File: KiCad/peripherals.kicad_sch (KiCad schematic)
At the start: 36 parts, among them IC1 MIC5350-SGYMT-TR, J1 Conn_02x06_Counter_Clockwise, J2 USB_C_Receptacle_USB2.0_14P, J3 Conn_01x07, J4 Conn_01x06, J6 Conn_02x11_Counter_Clockwise, U1 EM008LX, U2 EM008LX, U3 EM008LX, X1 2x5 0.05" SWD

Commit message: update draft to 11/13 version
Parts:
- removed J6: Conn_02x11_Counter_Clockwise, Connector_Hirose:Hirose_DF11-22DP-2DSA_2x11_P2.00mm_Vertical, symbol Connector_Generic:Conn_02x11_Counter_Clockwise
- added C5, C6, C7, C8: 0.1 uF, Capacitor_SMD:C_0201_0603Metric, symbol Device:C
- added R16, R17: 10K, Resistor_SMD:R_0603_1608Metric, symbol Device:R
- added U5, U6: TXS0108EPW, Package_SO:TSSOP-20_4.4x6.5mm_P0.65mm, symbol Logic_LevelTranslator:TXS0108EPW
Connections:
- net 1V8: now also R4.2, R5.2, R6.2, C5.1, C8.1, U5.2 (VCCA), U6.2 (VCCA); no longer R4.1, R5.1, R6.1
- net 3V3: now also C6.1, C7.1, U5.19 (VCCB), U6.19 (VCCB)
- net GND: now also C5.2, C6.2, C7.2, C8.2, R16.2, R17.2, U5.11 (GND), U6.11 (GND)
- net PC04: now also U5.20 (B1); no longer U1.1 (~{CS})
- net PC05: now also U5.18 (B2); no longer R4.2, U1.7 (IO3/~{RESET})
- net PC06: now also U5.17 (B3); no longer U2.1 (~{CS})
- net PC07: now also U5.16 (B4); no longer R5.2, U2.7 (IO3/~{RESET})
- net PC10: now also U5.15 (B5); no longer R6.2, U3.7 (IO3/~{RESET})
- net PC11: now also U5.14 (B6); no longer U3.1 (~{CS})
- net PC12: now also U6.14 (B6); no longer R3.2, U3.3 (~{WP}/IO2)
- net PC14: now also U6.15 (B5); no longer R1.2, U1.3 (~{WP}/IO2)
- net PC15: now also U6.16 (B4); no longer R2.2, U2.3 (~{WP}/IO2)
- net PD08 (MOSI): now also U6.17 (B3); no longer U1.5 (IO0), U2.5 (IO0), U3.5 (IO0)
- net PD09 (SCK): now also U6.18 (B2); no longer U1.6 (CK), U2.6 (CK), U3.6 (CK)
- net PD11 (MISO): now also U6.20 (B1); no longer U1.2 (IO1), U2.2 (IO1), U3.2 (IO1)
- new net: R16.1, U5.10 (OE)
- new net: R17.1, U6.10 (OE)
- new net PC04 1V8: U1.1 (~{CS}), U5.1 (A1)
- new net PC05 1V8: R4.1, U1.7 (IO3/~{RESET}), U5.3 (A2)
- new net PC06 1V8: U2.1 (~{CS}), U5.4 (A3)
- new net PC07 1V8: R5.1, U2.7 (IO3/~{RESET}), U5.5 (A4)
- new net PC10 1V8: R6.1, U3.7 (IO3/~{RESET}), U5.6 (A5)
- new net PC11 1V8: U3.1 (~{CS}), U5.7 (A6)
- new net PC12 1V8: R3.2, U3.3 (~{WP}/IO2), U6.7 (A6)
- new net PC14 1V8: R1.2, U1.3 (~{WP}/IO2), U6.6 (A5)
- new net PC15 1V8: R2.2, U2.3 (~{WP}/IO2), U6.5 (A4)
- new net PD08 (MOSI) 1V8: U1.5 (IO0), U2.5 (IO0), U3.5 (IO0), U6.4 (A3)
- new net PD09 (SCK) 1V8: U1.6 (CK), U2.6 (CK), U3.6 (CK), U6.3 (A2)
- new net PD11 (MISO) 1V8: U1.2 (IO1), U2.2 (IO1), U3.2 (IO1), U6.1 (A1)
- no-connect marks 3 -> 11
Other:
- note removed: "PHOTODIODES"
- moved on the sheet: C1, H1, H2, H3, H4, J1, J2, ON1, R8, U1, U2, U3

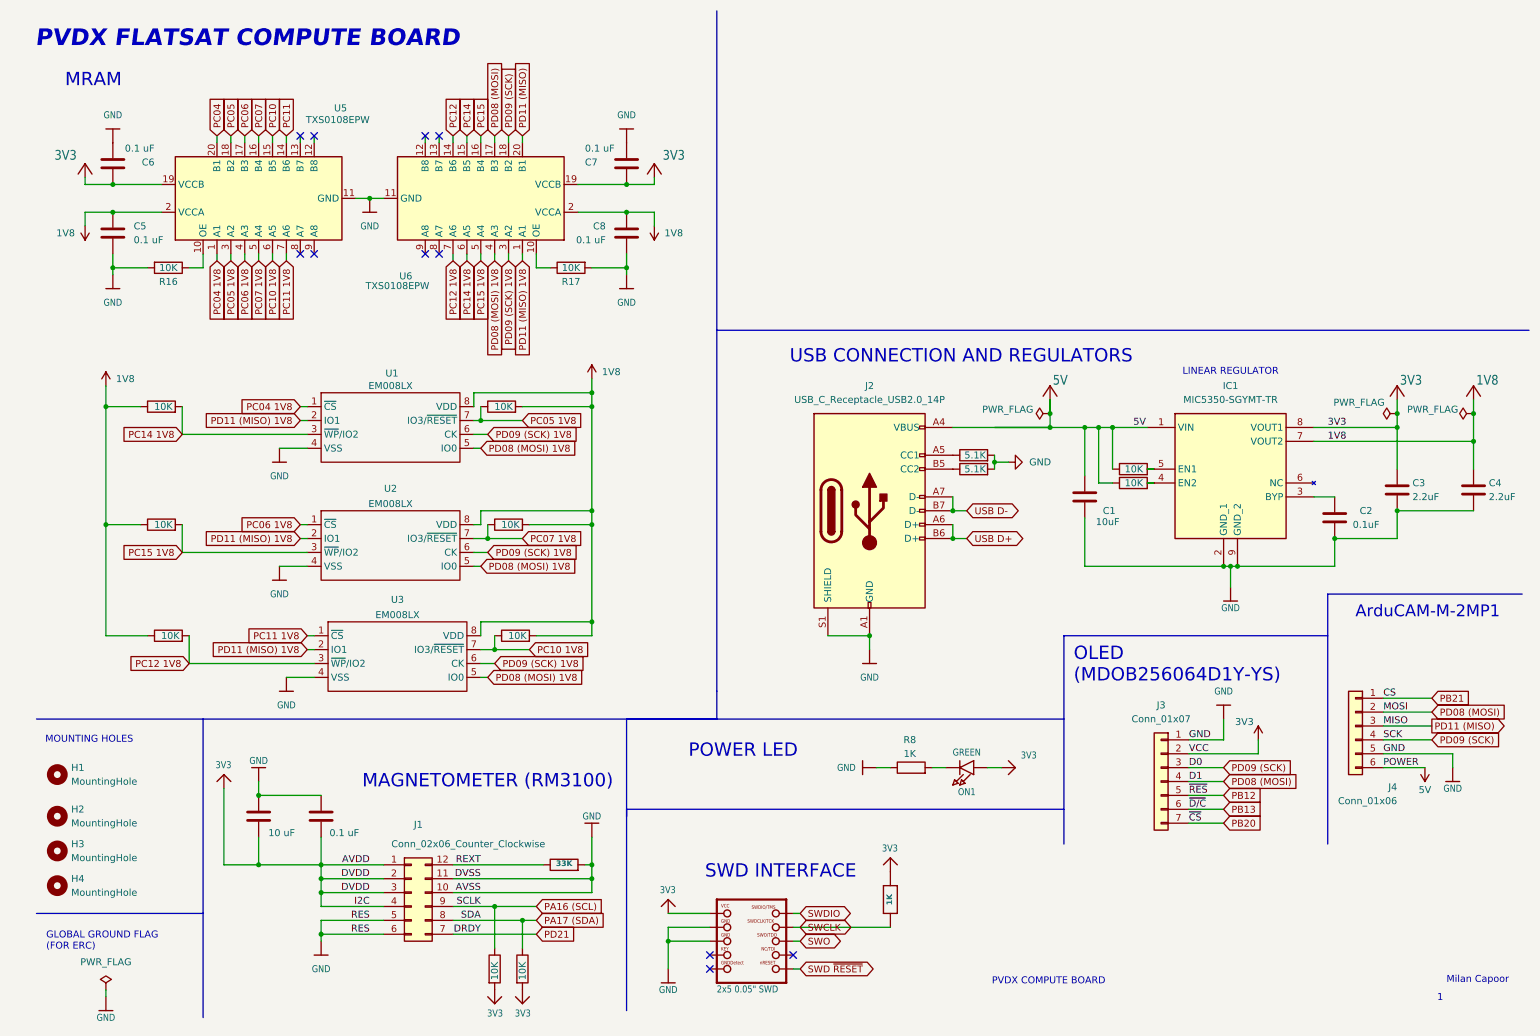
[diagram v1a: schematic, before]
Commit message: updated pins to match new spec and exposed all pins
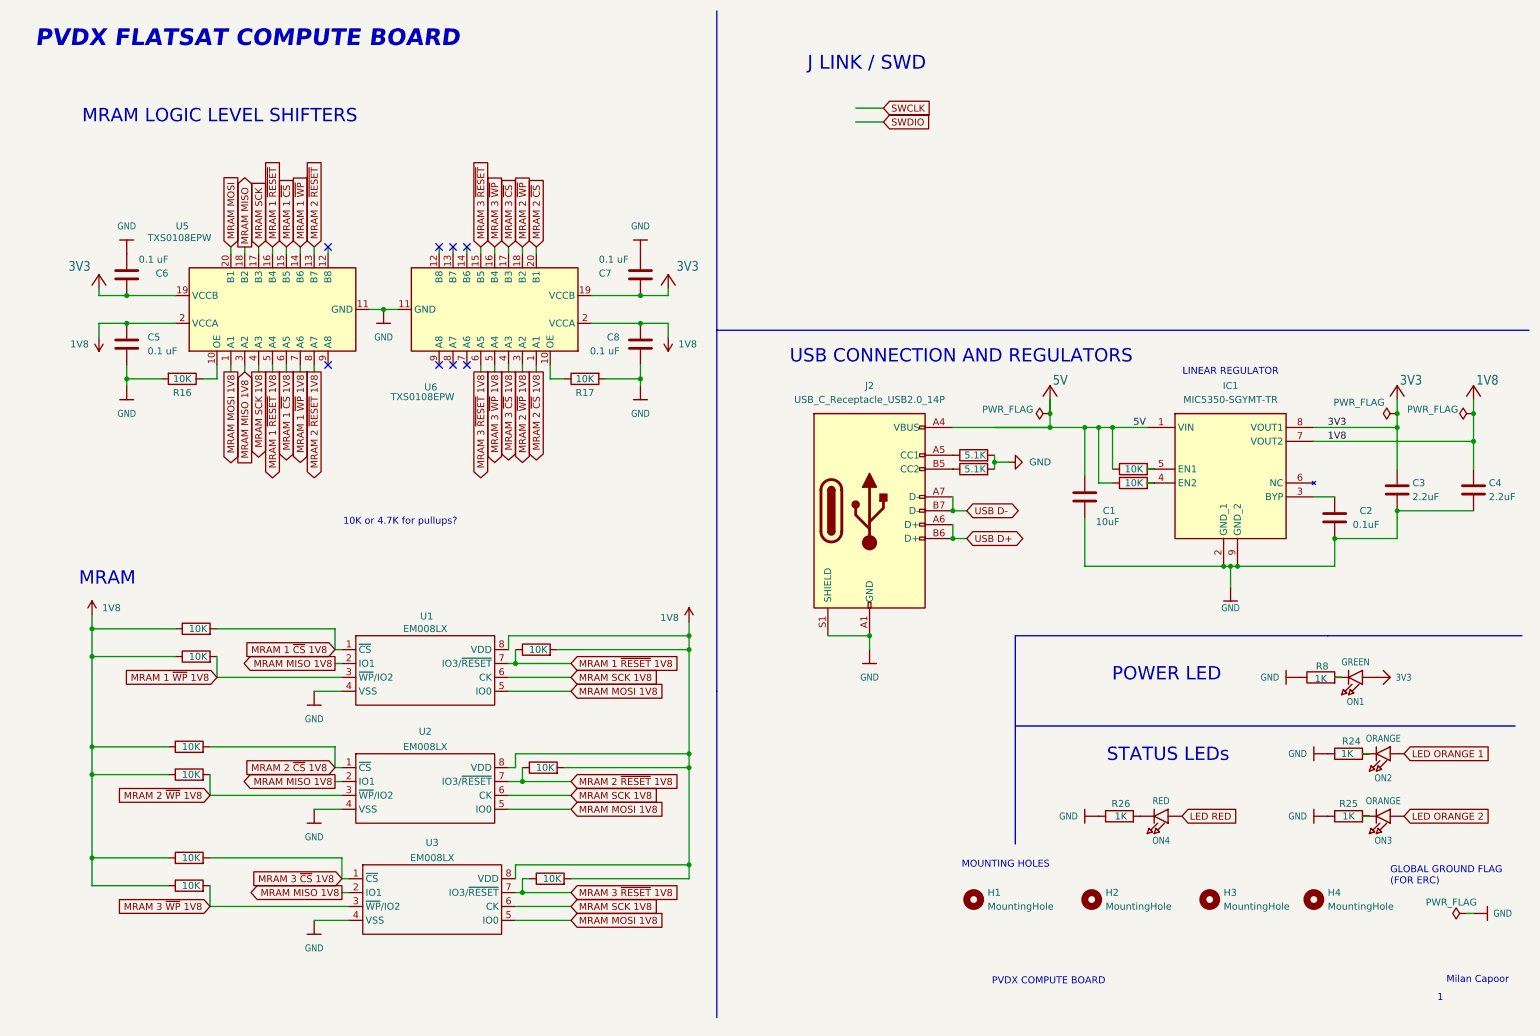
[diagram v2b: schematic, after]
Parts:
- removed CIN1: 10 uF, Capacitor_SMD:C_0201_0603Metric, symbol Device:C
- removed CIN2: 0.1 uF, Capacitor_SMD:C_0201_0603Metric, symbol Device:C
- removed J1: Conn_02x06_Counter_Clockwise, Connector_Harwin:Harwin_Gecko-G125-FVX1205L0X_2x06_P1.25mm_Vertical, symbol Connector_Generic:Conn_02x06_Counter_Clockwise
- removed J3: Conn_01x07, Connector_Molex:Molex_Micro-Latch_53253-0770_1x07_P2.00mm_Vertical, symbol Connector_Generic:Conn_01x07
- removed J4: Conn_01x06, Connector_Molex:Molex_Micro-Latch_53253-0670_1x06_P2.00mm_Vertical, symbol Connector_Generic:Conn_01x06
- removed R11: 1K, Resistor_SMD:R_0603_1608Metric, symbol Adafruit Grand Central M4 Express rev B-eagle-import:RESISTOR_0603_NOOUT
- removed R14, R15: 10K, Resistor_SMD:R_0603_1608Metric, symbol Device:R
- removed R7: 33K, Resistor_SMD:R_0603_1608Metric, symbol Device:R
- removed X1: 2x5 0.05" SWD, Adafruit Grand Central M4 Express rev B:2X05_1.27MM_BOX_POSTS, symbol Adafruit Grand Central M4 Express rev B-eagle-import:JTAG-CORTEXBOXPOSTS
- added ON2, ON3: ORANGE, Adafruit Grand Central M4 Express rev B:CHIPLED_0805_NOOUTLINE, symbol Adafruit Grand Central M4 Express rev B-eagle-import:LED0805_NOOUTLINE
- added ON4: RED, Adafruit Grand Central M4 Express rev B:CHIPLED_0805_NOOUTLINE, symbol Adafruit Grand Central M4 Express rev B-eagle-import:LED0805_NOOUTLINE
- added R11, R22, R23: 10K, Resistor_SMD:R_0603_1608Metric, symbol Device:R
- added R24, R25, R26: 1K, Resistor_SMD:R_0603_1608Metric, symbol Device:R
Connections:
- net 1V8: now also R11.1, R22.1, R23.1
- net GND: now also R24.1, R25.1, R26.1
- net MRAM 2 ~{RESET}: now reaches U5.13 (B7)
- net MRAM 2 ~{RESET} 1V8: now reaches U5.8 (A7)
- net MRAM 2 ~{RESET} 1V8: now also R5.1, U2.7 (IO3/~{RESET})
- net PC04 renamed MRAM MOSI
- net PC04 1V8 renamed MRAM 1 ~{CS} 1V8
- net MRAM 1 ~{CS} 1V8: now also U5.6 (A5), R11.2; no longer U5.1 (A1)
- net PC05 renamed MRAM MISO
- net PC05 1V8 renamed MRAM 1 ~{RESET} 1V8
- net MRAM 1 ~{RESET} 1V8: now also U5.5 (A4); no longer U5.3 (A2)
- net PC06 renamed MRAM SCK
- net PC06 1V8 renamed MRAM 2 ~{CS} 1V8
- net MRAM 2 ~{CS} 1V8: now also U6.1 (A1), R22.2; no longer U5.4 (A3)
- net PC07 renamed MRAM 1 ~{RESET}
- removed net PC07 1V8: R5.1, U2.7 (IO3/~{RESET}), U5.5 (A4)
- net PC10 renamed MRAM 1 ~{CS}
- net PC10 1V8 renamed MRAM 3 ~{RESET} 1V8
- net MRAM 3 ~{RESET} 1V8: now also U6.6 (A5); no longer U5.6 (A5)
- net PC11 renamed MRAM 1 ~{WP}
- net PC11 1V8 renamed MRAM 1 ~{WP} 1V8
- net MRAM 1 ~{WP} 1V8: now also R1.2, U1.3 (~{WP}/IO2); no longer U3.1 (~{CS})
- net PC12: no longer names the net of U6.14 (B6)
- net PC12 1V8 renamed MRAM 3 ~{WP} 1V8
- net MRAM 3 ~{WP} 1V8: now also U6.5 (A4); no longer U6.7 (A6)
- net PC14 renamed MRAM 3 ~{RESET}
- removed net PC14 1V8: R1.2, U1.3 (~{WP}/IO2), U6.6 (A5)
- net PC15 renamed MRAM 3 ~{WP}
- net PC15 1V8 renamed MRAM 2 ~{WP} 1V8
- net MRAM 2 ~{WP} 1V8: now also U6.3 (A2); no longer U6.5 (A4)
- net PD08 (MOSI) renamed MRAM 3 ~{CS}
- net PD08 (MOSI) 1V8 renamed MRAM MOSI 1V8
- net MRAM MOSI 1V8: now also U5.1 (A1); no longer U6.4 (A3)
- net PD09 (SCK) renamed MRAM 2 ~{WP}
- net PD09 (SCK) 1V8 renamed MRAM SCK 1V8
- net MRAM SCK 1V8: now also U5.4 (A3); no longer U6.3 (A2)
- net PD11 (MISO) renamed MRAM 2 ~{CS}
- net PD11 (MISO) 1V8 renamed MRAM MISO 1V8
- net MRAM MISO 1V8: now also U5.3 (A2); no longer U6.1 (A1)
- new net: ON2.C, R24.2
- new net: ON4.C, R26.2
- new net: ON3.C, R25.2
- new net LED ORANGE 1: ON2.A
- new net LED ORANGE 2: ON3.A
- new net LED RED: ON4.A
- new net MRAM 3 ~{CS} 1V8: R23.2, U3.1 (~{CS}), U6.4 (A3)
- no-connect marks 11 -> 8
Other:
- note added: "10K or 4.7K for pullups?"
- note added: "J LINK / SWD"
- note added: "MRAM LOGIC LEVEL SHIFTERS"
- note added: "STATUS LEDs"
- note removed: "ArduCAM-M-2MP1"
- note removed: "MAGNETOMETER (RM3100)"
- note removed: "OLED (MDOB256064D1Y-YS)"
- note removed: "SWD INTERFACE"
- moved on the sheet: C5, C6, C7, C8, H1, H2, H3, H4, ON1, R16, R17, R8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
